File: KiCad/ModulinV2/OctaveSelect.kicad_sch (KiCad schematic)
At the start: 37 parts, among them IC30 SN74LV10ADR, IC31 SN74LV10ADR, IC32 SN74LV10ADR, IC33 SN74HC193DR, IC34 TMUX4051DYYRQ1, IC35 TL072HIDR, SW2 Rocker Switch

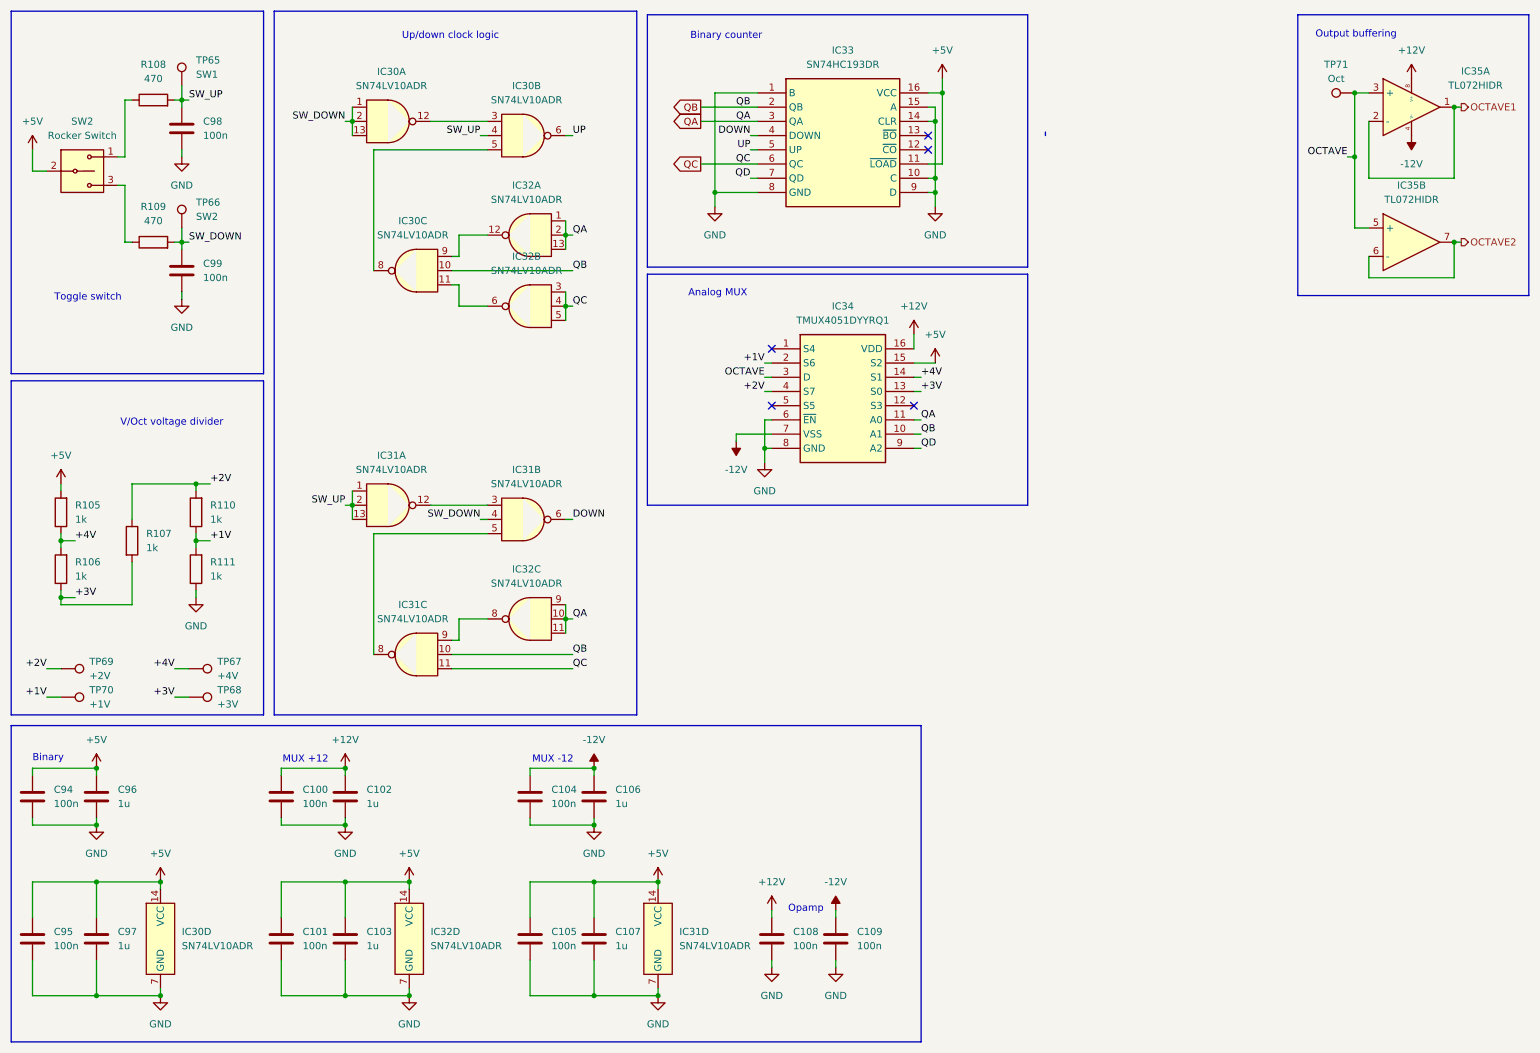
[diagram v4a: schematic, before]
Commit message: Added footprints to all capacitors and potentiometers
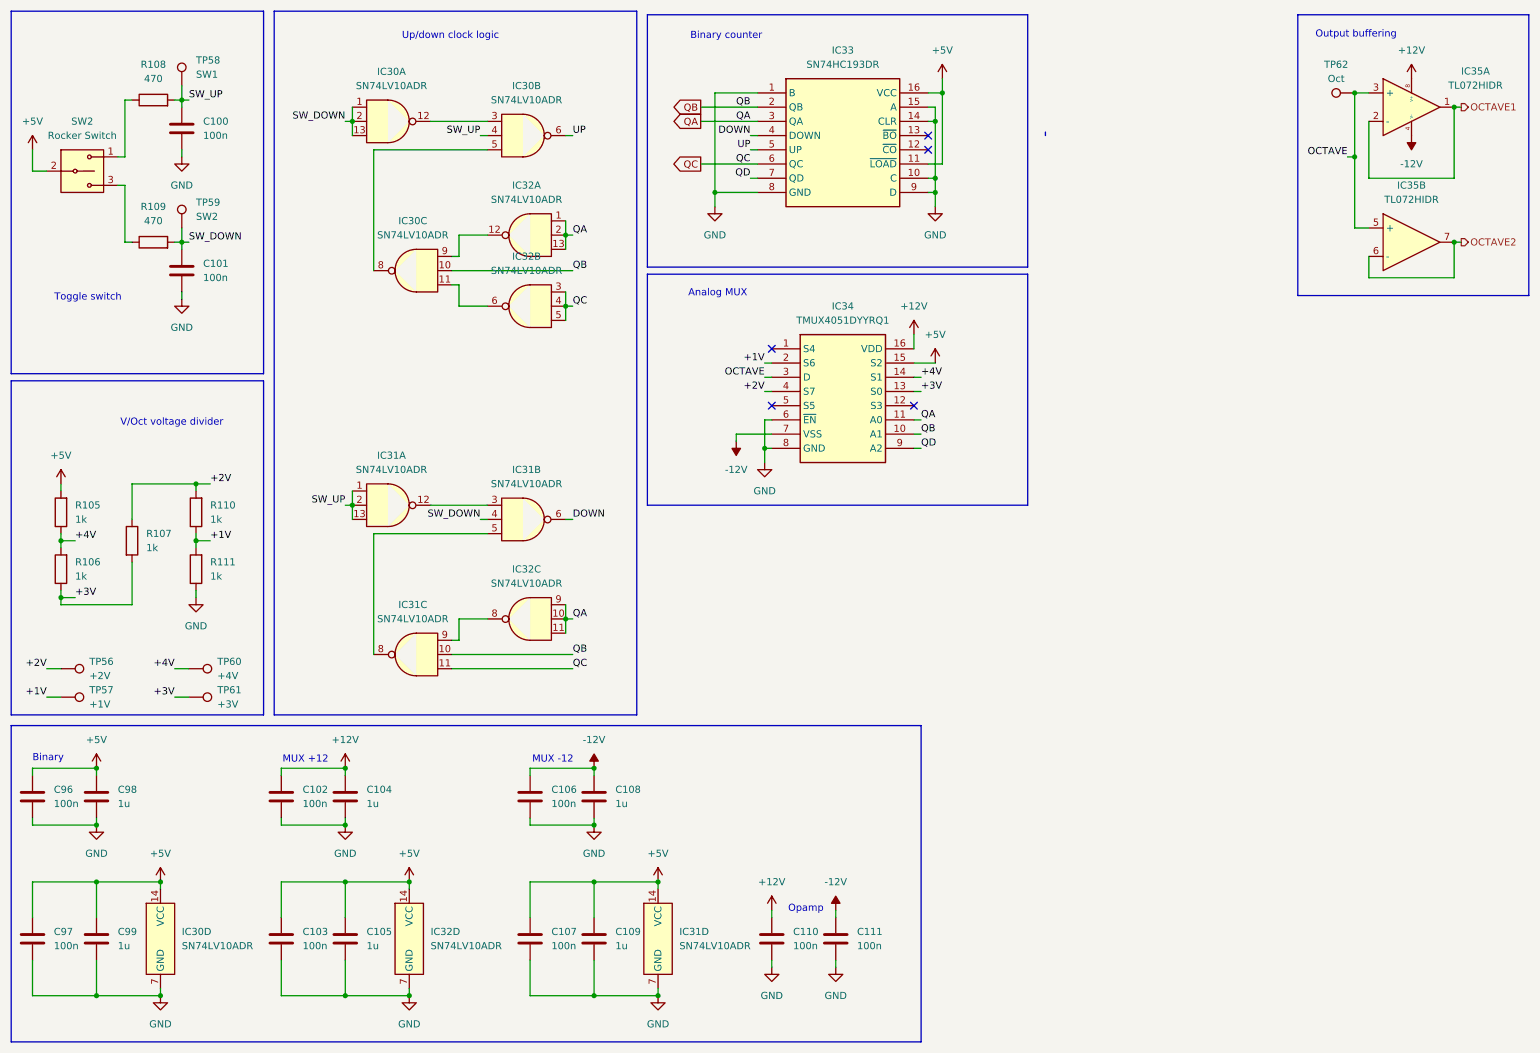
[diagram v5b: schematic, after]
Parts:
- C100: renamed from C98; footprint SamacSys_Parts:CAPC1608X90N -> Capacitor_SMD:C_0603_1608Metric_Pad1.08x0.95mm_HandSolder
- C101: renamed from C99; footprint SamacSys_Parts:CAPC1608X90N -> Capacitor_SMD:C_0603_1608Metric_Pad1.08x0.95mm_HandSolder
- C102: renamed from C100; footprint SamacSys_Parts:CAPC1608X90N -> Capacitor_SMD:C_0603_1608Metric_Pad1.08x0.95mm_HandSolder
- C103: renamed from C101; footprint SamacSys_Parts:CAPC1608X90N -> Capacitor_SMD:C_0603_1608Metric_Pad1.08x0.95mm_HandSolder
- C104: renamed from C102; footprint SamacSys_Parts:CAPC1608X95N -> Capacitor_SMD:C_0603_1608Metric_Pad1.08x0.95mm_HandSolder
- C105: renamed from C103; footprint SamacSys_Parts:CAPC1608X95N -> Capacitor_SMD:C_0603_1608Metric_Pad1.08x0.95mm_HandSolder
- C106: renamed from C104; footprint SamacSys_Parts:CAPC1608X90N -> Capacitor_SMD:C_0603_1608Metric_Pad1.08x0.95mm_HandSolder
- C107: renamed from C105; footprint SamacSys_Parts:CAPC1608X90N -> Capacitor_SMD:C_0603_1608Metric_Pad1.08x0.95mm_HandSolder
- C108: renamed from C106; footprint SamacSys_Parts:CAPC1608X95N -> Capacitor_SMD:C_0603_1608Metric_Pad1.08x0.95mm_HandSolder
- C109: renamed from C107; footprint SamacSys_Parts:CAPC1608X95N -> Capacitor_SMD:C_0603_1608Metric_Pad1.08x0.95mm_HandSolder
- C110: renamed from C108; footprint SamacSys_Parts:CAPC1608X90N -> Capacitor_SMD:C_0603_1608Metric_Pad1.08x0.95mm_HandSolder
- C111: renamed from C109; footprint SamacSys_Parts:CAPC1608X90N -> Capacitor_SMD:C_0603_1608Metric_Pad1.08x0.95mm_HandSolder
- C96: renamed from C94; footprint SamacSys_Parts:CAPC1608X90N -> Capacitor_SMD:C_0603_1608Metric_Pad1.08x0.95mm_HandSolder
- C97: renamed from C95; footprint SamacSys_Parts:CAPC1608X90N -> Capacitor_SMD:C_0603_1608Metric_Pad1.08x0.95mm_HandSolder
- C98: renamed from C96; footprint SamacSys_Parts:CAPC1608X95N -> Capacitor_SMD:C_0603_1608Metric_Pad1.08x0.95mm_HandSolder
- C99: renamed from C97; footprint SamacSys_Parts:CAPC1608X95N -> Capacitor_SMD:C_0603_1608Metric_Pad1.08x0.95mm_HandSolder
- renumbered TP69 to TP56, TP70 to TP57, TP65 to TP58, TP66 to TP59, TP67 to TP60, TP68 to TP61, TP71 to TP62

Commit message: Finished Schematic, started on PCB
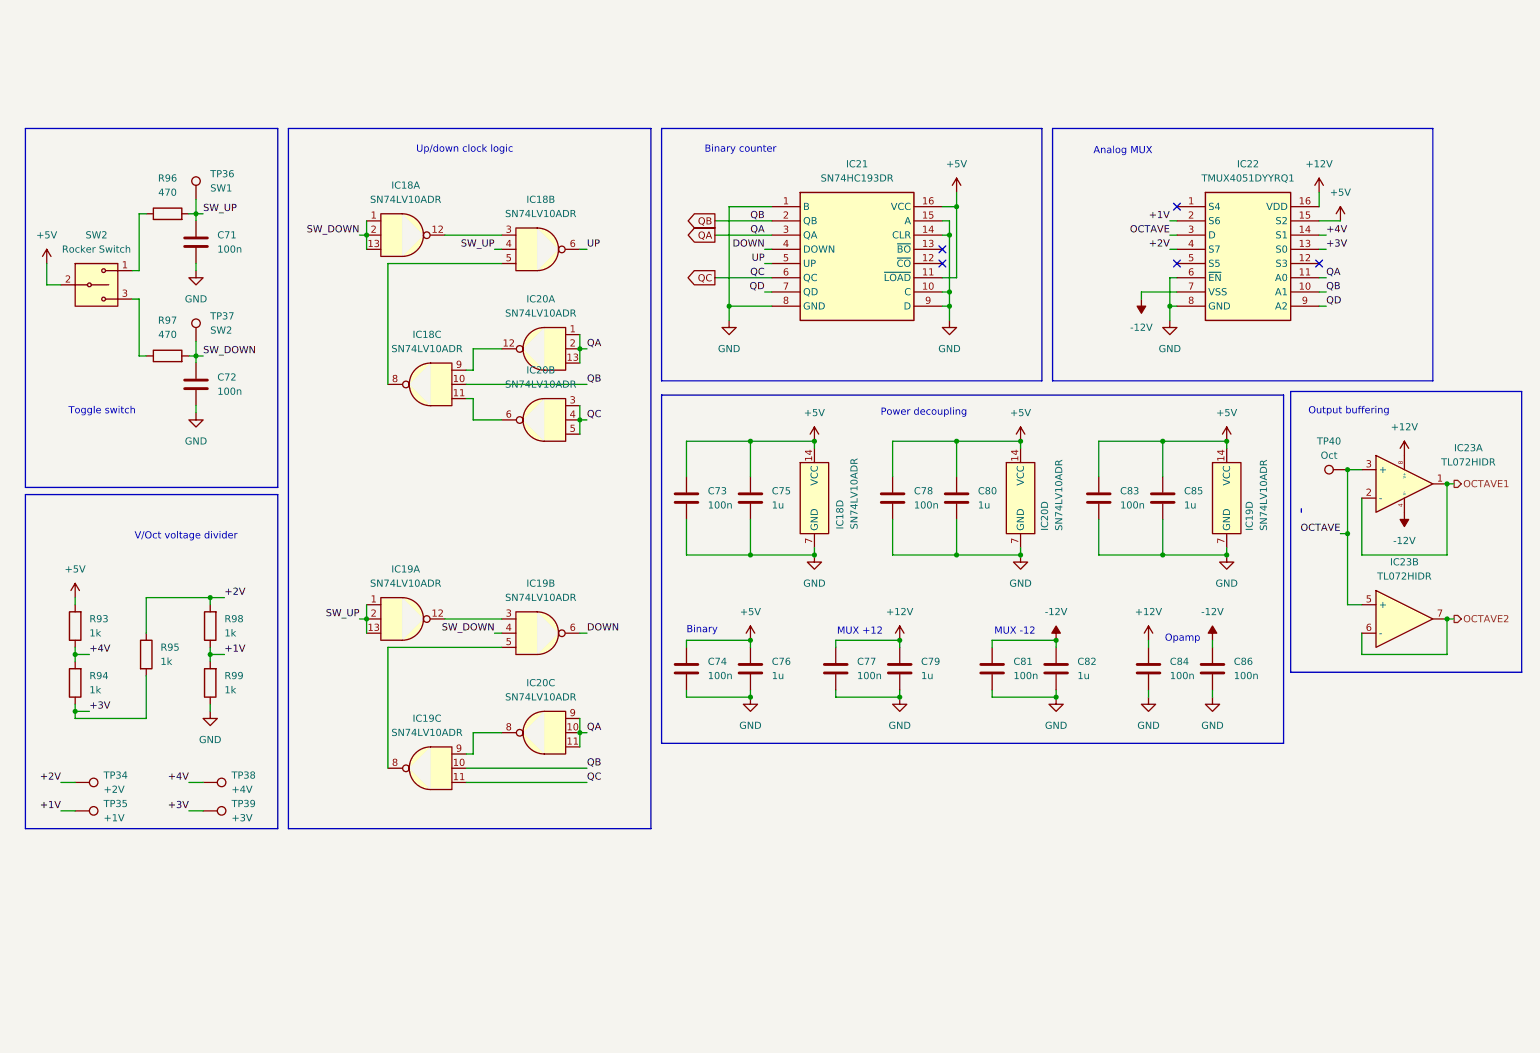
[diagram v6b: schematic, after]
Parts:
- R93: renamed from R105; footprint (none) -> Resistor_SMD:R_0603_1608Metric_Pad0.98x0.95mm_HandSolder
- R94: renamed from R106; footprint (none) -> Resistor_SMD:R_0603_1608Metric_Pad0.98x0.95mm_HandSolder
- R95: renamed from R107; footprint (none) -> Resistor_SMD:R_0603_1608Metric_Pad0.98x0.95mm_HandSolder
- R96: renamed from R108; footprint (none) -> Resistor_SMD:R_0603_1608Metric_Pad0.98x0.95mm_HandSolder
- R97: renamed from R109; footprint (none) -> Resistor_SMD:R_0603_1608Metric_Pad0.98x0.95mm_HandSolder
- R98: renamed from R110; footprint (none) -> Resistor_SMD:R_0603_1608Metric_Pad0.98x0.95mm_HandSolder
- R99: renamed from R111; footprint (none) -> Resistor_SMD:R_0603_1608Metric_Pad0.98x0.95mm_HandSolder
- renumbered C100 to C71, C101 to C72, C97 to C73, C96 to C74, C99 to C75, C98 to C76, C102 to C77, C103 to C78, C104 to C79, C105 to C80, C106 to C81, C108 to C82, C107 to C83, C110 to C84, C109 to C85, C111 to C86, IC30 to IC18, IC31 to IC19, IC32 to IC20, IC33 to IC21, IC34 to IC22, IC35 to IC23, TP56 to TP34, TP57 to TP35, TP58 to TP36, TP59 to TP37, TP60 to TP38, TP61 to TP39, TP62 to TP40
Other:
- note added: "Power decoupling"
- moved on the sheet: C71, C72, C73, C74, C75, C76, C77, C78, C79, C80, C81, C82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

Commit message: Layed out Interface and PWR components and started with MCU layout
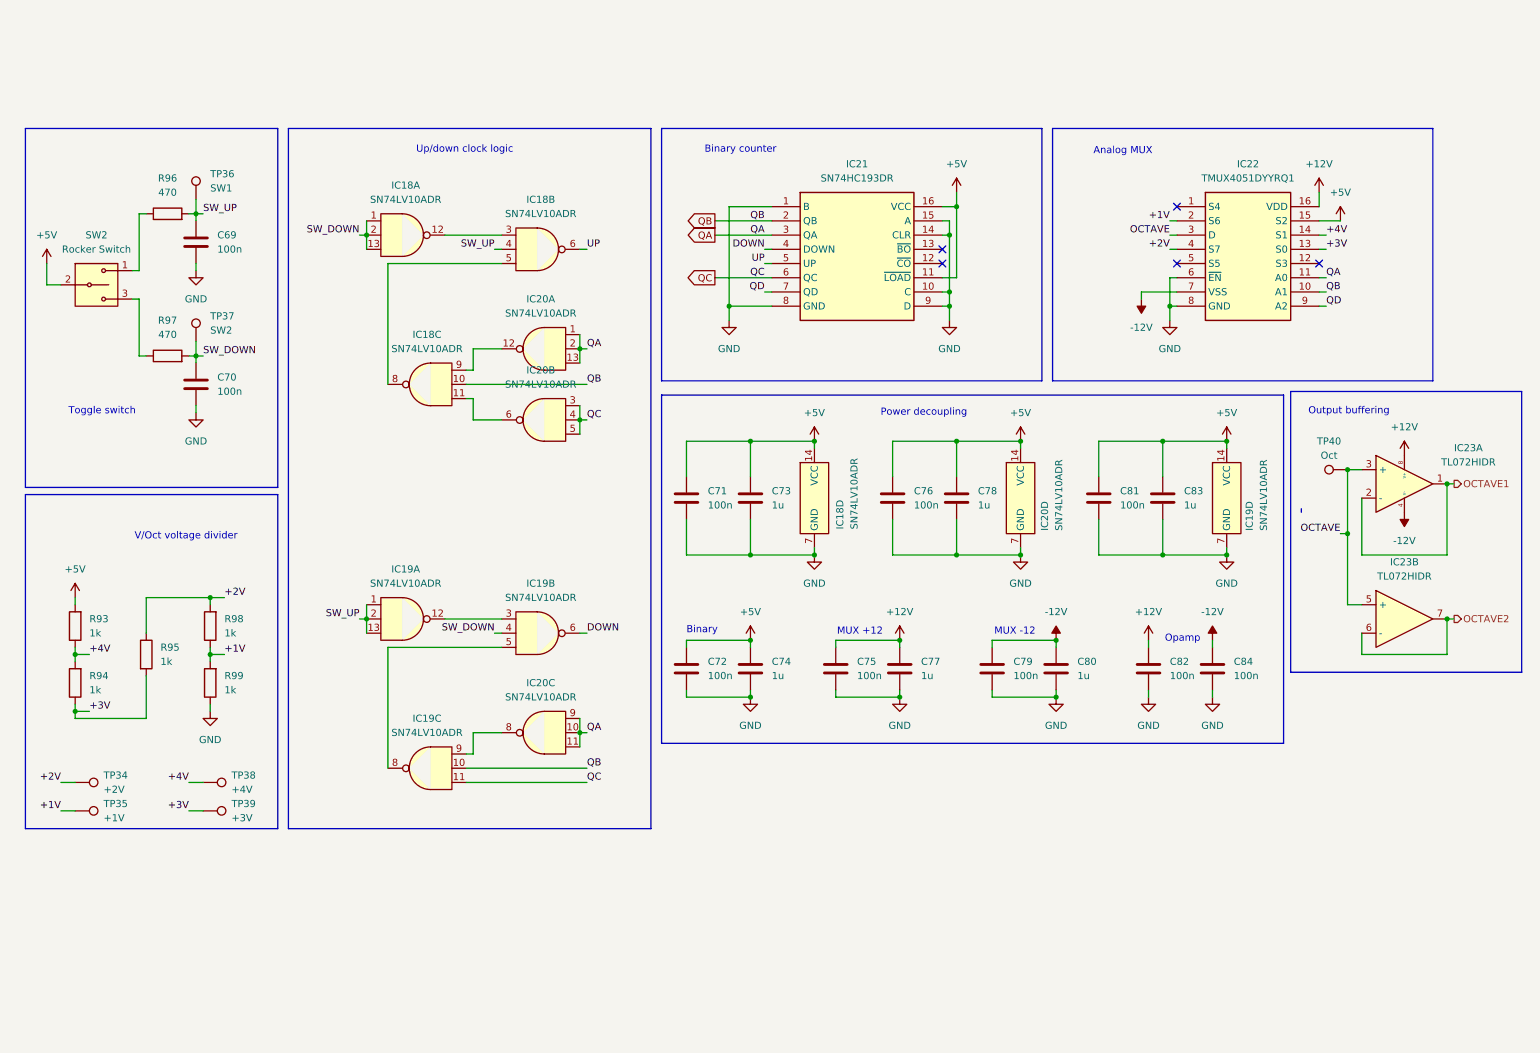
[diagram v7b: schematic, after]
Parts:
- renumbered C71 to C69, C72 to C70, C73 to C71, C74 to C72, C75 to C73, C76 to C74, C77 to C75, C78 to C76, C79 to C77, C80 to C78, C81 to C79, C82 to C80, C83 to C81, C84 to C82, C85 to C83, C86 to C84
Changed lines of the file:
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@@
 		(dnp no)
 		(fields_autoplaced yes)
-		(property "Reference" "C77"
+		(property "Reference" "C75"
 			(at 163.83 129.5399 0)
 			(effects
@@
 			(project "ModulinV2"
 				(path "/c6b34a57-3941-4b56-8b80-1848c7f41082/3ee27ced-353d-4052-9ca0-cd235d9ddb69/9bc61cdb-3471-4563-89f4-fea731357cf2"
-					(reference "C77")
+					(reference "C75")
 					(unit 1)
 				)
@@
 		(dnp no)
 		(fields_autoplaced yes)
-		(property "Reference" "C76"
+		(property "Reference" "C74"
 			(at 148.59 129.5399 0)
 			(effects
@@
 			(project "ModulinV2"
 				(path "/c6b34a57-3941-4b56-8b80-1848c7f41082/3ee27ced-353d-4052-9ca0-cd235d9ddb69/9bc61cdb-3471-4563-89f4-fea731357cf2"
-					(reference "C76")
+					(reference "C74")
 					(unit 1)
 				)
@@
 		(dnp no)
 		(fields_autoplaced yes)
-		(property "Reference" "C79"
+		(property "Reference" "C77"
 			(at 175.26 129.5399 0)
 			(effects
@@
 			(project "ModulinV2"
 				(path "/c6b34a57-3941-4b56-8b80-1848c7f41082/3ee27ced-353d-4052-9ca0-cd235d9ddb69/9bc61cdb-3471-4563-89f4-fea731357cf2"
-					(reference "C79")
+					(reference "C77")
 					(unit 1)
 				)
@@
 		(dnp no)
 		(fields_autoplaced yes)
-		(property "Reference" "C78"
+		(property "Reference" "C76"
 			(at 173.99 99.0599 0)
 			(effects
@@
 			(project "ModulinV2"
 				(path "/c6b34a57-3941-4b56-8b80-1848c7f41082/3ee27ced-353d-4052-9ca0-cd235d9ddb69/9bc61cdb-3471-4563-89f4-fea731357cf2"
-					(reference "C78")
+					(reference "C76")
 					(unit 1)
 				)
@@
 		(dnp no)
 		(fields_autoplaced yes)
-		(property "Reference" "C84"
+		(property "Reference" "C82"
 			(at 219.71 129.5399 0)
 			(effects
@@
 			(project "ModulinV2"
 				(path "/c6b34a57-3941-4b56-8b80-1848c7f41082/3ee27ced-353d-4052-9ca0-cd235d9ddb69/9bc61cdb-3471-4563-89f4-fea731357cf2"
-					(reference "C84")
+					(reference "C82")
 					(unit 1)
 				)
@@
 		(dnp no)
 		(fields_autoplaced yes)
-		(property "Reference" "C71"
+		(property "Reference" "C69"
 			(at 49.53 53.3399 0)
 			(effects
@@
 			(project "ModulinV2"
 				(path "/c6b34a57-3941-4b56-8b80-1848c7f41082/3ee27ced-353d-4052-9ca0-cd235d9ddb69/9bc61cdb-3471-4563-89f4-fea731357cf2"
-					(reference "C71")
+					(reference "C69")
 					(unit 1)
 				)
@@
 		(dnp no)
 		(fields_autoplaced yes)
-		(property "Reference" "C72"
+		(property "Reference" "C70"
 			(at 49.53 78.7399 0)
 			(effects
@@
 			(project "ModulinV2"
 				(path "/c6b34a57-3941-4b56-8b80-1848c7f41082/3ee27ced-353d-4052-9ca0-cd235d9ddb69/9bc61cdb-3471-4563-89f4-fea731357cf2"
-					(reference "C72")
+					(reference "C70")
 					(unit 1)
 				)
@@
 		(dnp no)
 		(fields_autoplaced yes)
-		(property "Reference" "C74"
+		(property "Reference" "C72"
 			(at 137.16 129.5399 0)
 			(effects
@@
 			(project "ModulinV2"
 				(path "/c6b34a57-3941-4b56-8b80-1848c7f41082/3ee27ced-353d-4052-9ca0-cd235d9ddb69/9bc61cdb-3471-4563-89f4-fea731357cf2"
-					(reference "C74")
+					(reference "C72")
 					(unit 1)
 				)
@@
 		(dnp no)
 		(fields_autoplaced yes)
-		(property "Reference" "C85"
+		(property "Reference" "C83"
 			(at 222.25 99.0599 0)
 			(effects
@@
 			(project "ModulinV2"
 				(path "/c6b34a57-3941-4b56-8b80-1848c7f41082/3ee27ced-353d-4052-9ca0-cd235d9ddb69/9bc61cdb-3471-4563-89f4-fea731357cf2"
-					(reference "C85")
+					(reference "C83")
 					(unit 1)
 				)
@@
 		(dnp no)
 		(fields_autoplaced yes)
-		(property "Reference" "C80"
+		(property "Reference" "C78"
 			(at 185.42 99.0599 0)
 			(effects
@@
 			(project "ModulinV2"
 				(path "/c6b34a57-3941-4b56-8b80-1848c7f41082/3ee27ced-353d-4052-9ca0-cd235d9ddb69/9bc61cdb-3471-4563-89f4-fea731357cf2"
-					(reference "C80")
+					(reference "C78")
 					(unit 1)
 				)
@@
 		(dnp no)
 		(fields_autoplaced yes)
-		(property "Reference" "C83"
+		(property "Reference" "C81"
 			(at 210.82 99.0599 0)
 			(effects
@@
 			(project "ModulinV2"
 				(path "/c6b34a57-3941-4b56-8b80-1848c7f41082/3ee27ced-353d-4052-9ca0-cd235d9ddb69/9bc61cdb-3471-4563-89f4-fea731357cf2"
-					(reference "C83")
+					(reference "C81")
 					(unit 1)
 				)
@@
 		(dnp no)
 		(fields_autoplaced yes)
-		(property "Reference" "C73"
+		(property "Reference" "C71"
 			(at 137.16 99.0599 0)
 			(effects
@@
 			(project "ModulinV2"
 				(path "/c6b34a57-3941-4b56-8b80-1848c7f41082/3ee27ced-353d-4052-9ca0-cd235d9ddb69/9bc61cdb-3471-4563-89f4-fea731357cf2"
-					(reference "C73")
+					(reference "C71")
 					(unit 1)
 				)
@@
 		(dnp no)
 		(fields_autoplaced yes)
-		(property "Reference" "C86"
+		(property "Reference" "C84"
 			(at 231.14 129.5399 0)
 			(effects
@@
 			(project "ModulinV2"
 				(path "/c6b34a57-3941-4b56-8b80-1848c7f41082/3ee27ced-353d-4052-9ca0-cd235d9ddb69/9bc61cdb-3471-4563-89f4-fea731357cf2"
-					(reference "C86")
+					(reference "C84")
 					(unit 1)
 				)
@@
 		(dnp no)
 		(fields_autoplaced yes)
-		(property "Reference" "C75"
+		(property "Reference" "C73"
 			(at 148.59 99.0599 0)
 			(effects
@@
 			(project "ModulinV2"
 				(path "/c6b34a57-3941-4b56-8b80-1848c7f41082/3ee27ced-353d-4052-9ca0-cd235d9ddb69/9bc61cdb-3471-4563-89f4-fea731357cf2"
-					(reference "C75")
+					(reference "C73")
 					(unit 1)
 				)
@@
 		(dnp no)
 		(fields_autoplaced yes)
-		(property "Reference" "C81"
+		(property "Reference" "C79"
 			(at 191.77 129.5399 0)
 			(effects
@@
 			(project "ModulinV2"
 				(path "/c6b34a57-3941-4b56-8b80-1848c7f41082/3ee27ced-353d-4052-9ca0-cd235d9ddb69/9bc61cdb-3471-4563-89f4-fea731357cf2"
-					(reference "C81")
+					(reference "C79")
 					(unit 1)
 				)
@@
 		(dnp no)
 		(fields_autoplaced yes)
-		(property "Reference" "C82"
+		(property "Reference" "C80"
 			(at 203.2 129.5399 0)
 			(effects
@@
 			(project "ModulinV2"
 				(path "/c6b34a57-3941-4b56-8b80-1848c7f41082/3ee27ced-353d-4052-9ca0-cd235d9ddb69/9bc61cdb-3471-4563-89f4-fea731357cf2"
-					(reference "C82")
+					(reference "C80")
 					(unit 1)
 				)
